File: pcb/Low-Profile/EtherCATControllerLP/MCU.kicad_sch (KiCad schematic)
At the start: 8 parts, among them U1 STM32F405RGT6, Y1 ABM3B-8.000MHZ-10-1-U-T

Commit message: checkpoint
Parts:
- U1: LCSC Part # (none) -> C15742; LCSC Part Number C15742 -> (none)
- Y1: LCSC Part # (none) -> C276420; LCSC Part Number C276420 -> (none)
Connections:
- net GND: now also U1.28 (PB2)
- net TEMP_MOSFETS: now reaches U1.15 (PA1)
- net TEMP_ICS: now reaches U1.16 (PA2)
- net TEMP_BACKSIDE: now reaches U1.17 (PA3)
- net VDD renamed VCC
- no-connect marks 19 -> 15

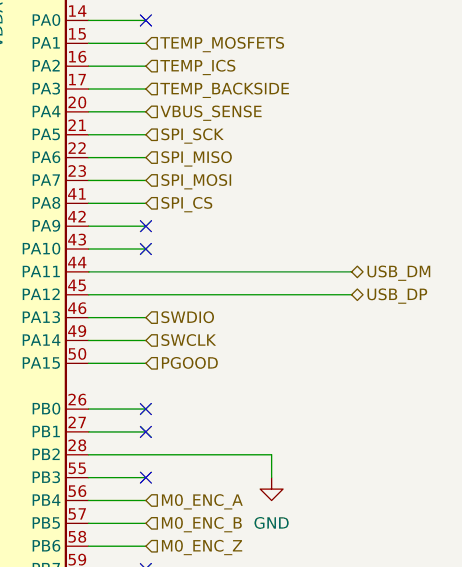
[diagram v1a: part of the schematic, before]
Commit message: Checkpoint changes before switching to XMC4800
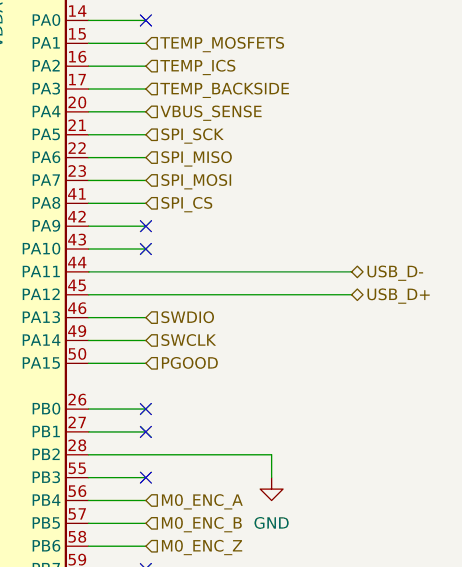
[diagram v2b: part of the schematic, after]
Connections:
- net USB_DM renamed USB_D-
- net USB_DP renamed USB_D+
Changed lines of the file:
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@@
 		)
 	)
-	(hierarchical_label "USB_DM"
+	(hierarchical_label "USB_D-"
 		(shape bidirectional)
 		(at 193.04 67.31 0)
@@
 		)
 	)
-	(hierarchical_label "USB_DP"
+	(hierarchical_label "USB_D+"
 		(shape bidirectional)
 		(at 193.04 69.85 0)

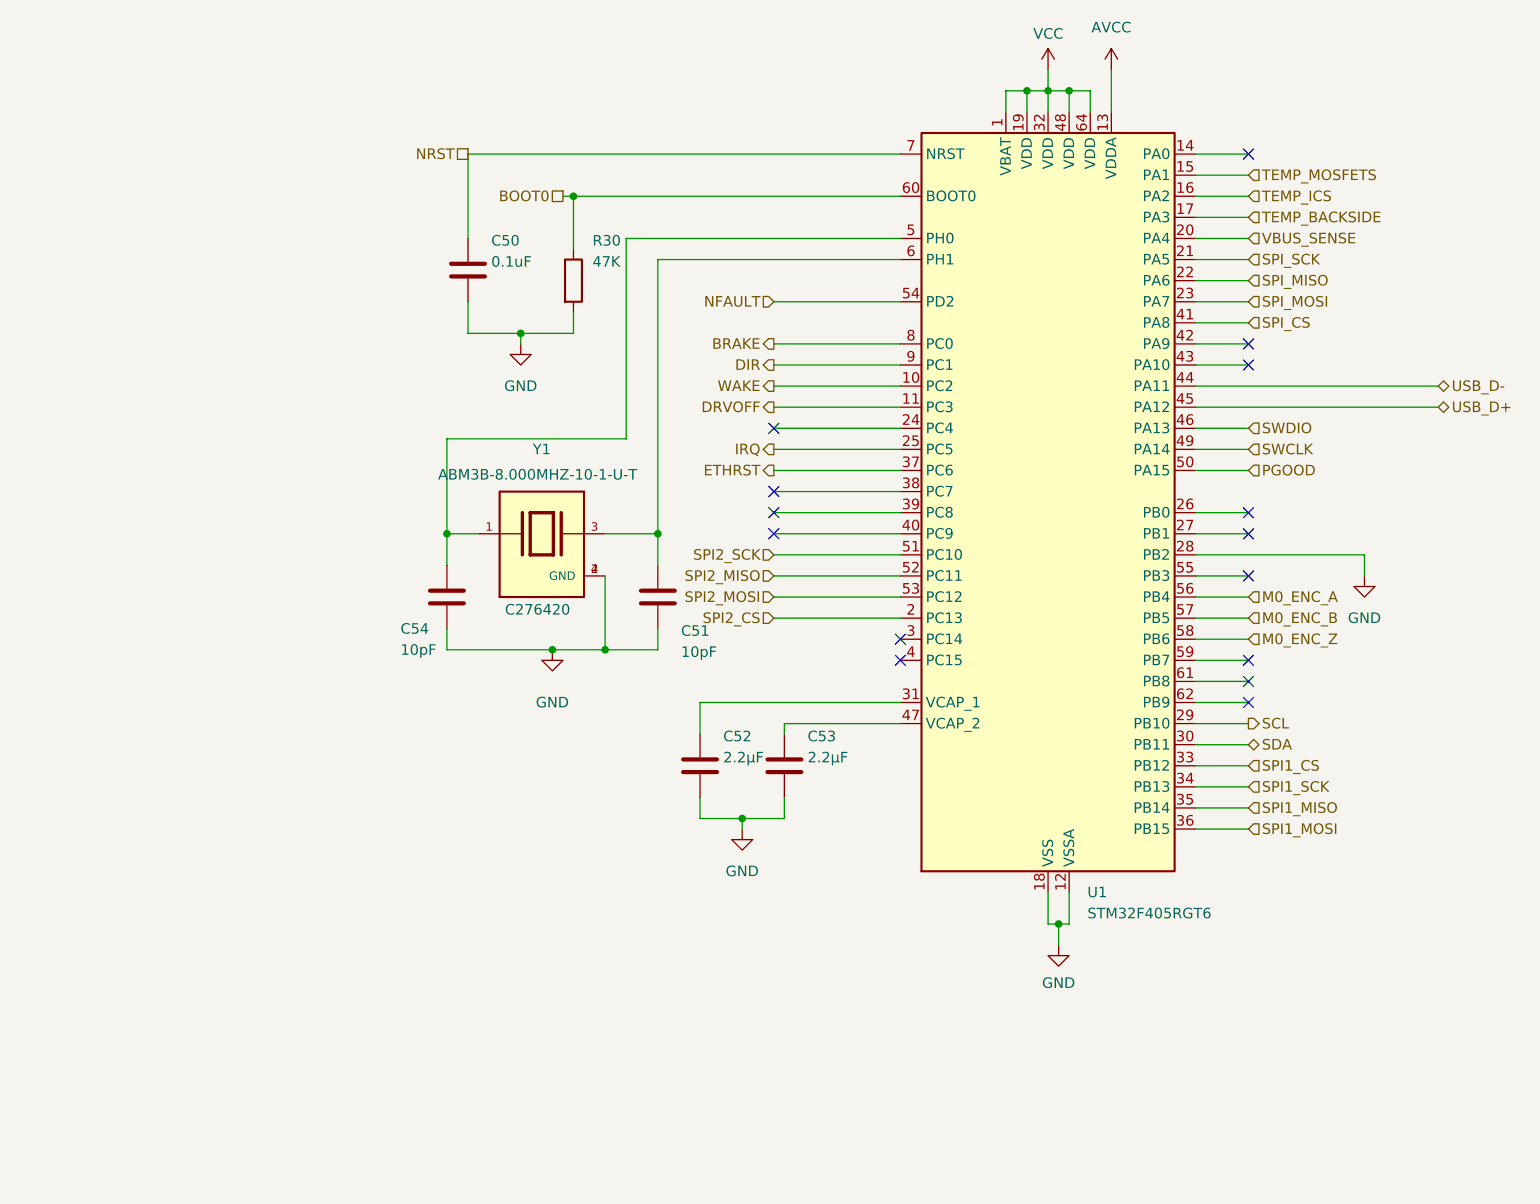
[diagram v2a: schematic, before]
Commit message: Added XMC4800
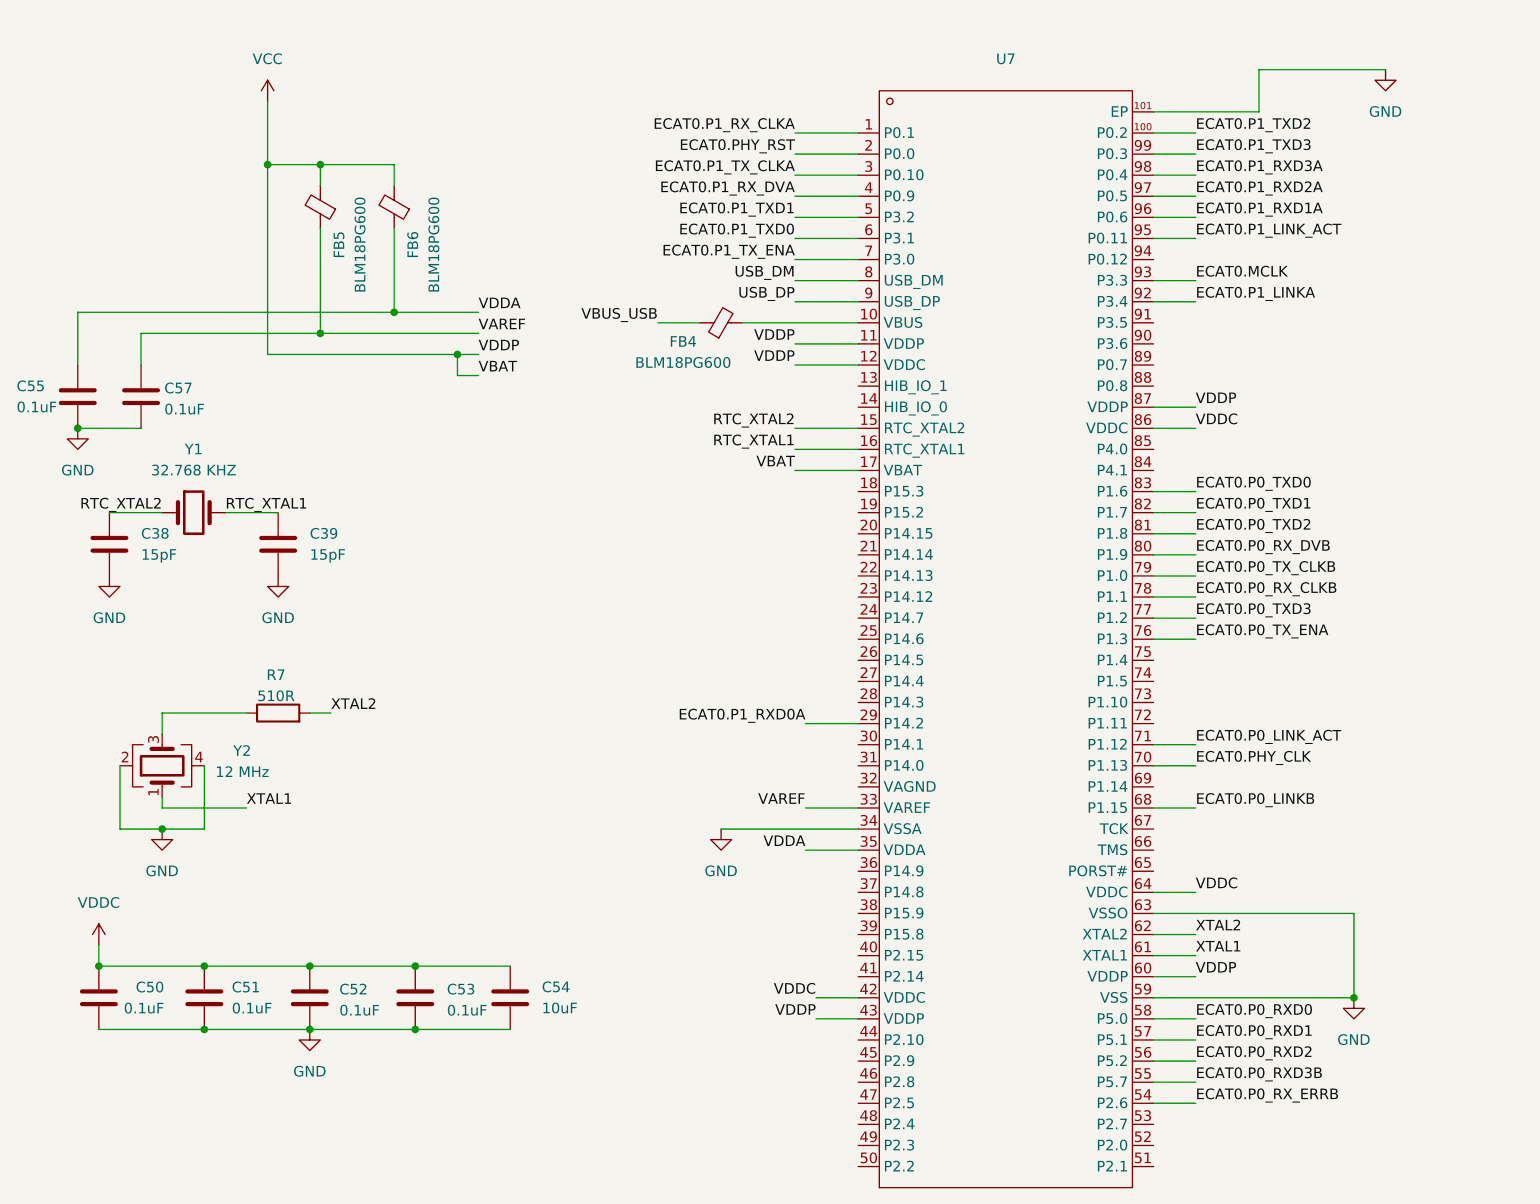
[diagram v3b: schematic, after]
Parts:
- removed R30: 47K, Resistor_SMD:R_0603_1608Metric, symbol Device:R
- removed U1: STM32F405RGT6, Package_QFP:LQFP-64_10x10mm_P0.5mm, symbol MCU_ST_STM32F4:STM32F405RGTx
- removed Y1: ABM3B-8.000MHZ-10-1-U-T, Crystal:Crystal_SMD_5032-4Pin_5.0x3.2mm, symbol ABM3B-8.000MHZ-10-1-U-T:ABM3B-8.000MHZ-10-1-U-T
- added C38, C39: 15pF, symbol Device:C
- added C55, C57: ${CAPACITANCE}, Capacitor_SMD:C_0603_1608Metric, symbol Device:C
- added FB4, FB5, FB6: BLM18PG600, symbol Device:FerriteBead_Small
- added R7: 510R, symbol Device:R
- added U7: ~, ProLibrary_pcs_2024-07-15:PG-LQFP-100_L14.0-W14.0-P0.50-LS16.0-BL-EP7.0, symbol XMC4800:XMC4800F100K1024AAXQMA1
- added Y1: 32.768 KHZ, SMD3215-2P, symbol Device:Crystal
- added Y2: 12 MHz, SMD3225-4P, symbol Device:Crystal_GND24
- C50: LCSC Part # (none) -> C77055
- C51: CAPACITANCE 10pF -> 0.1uF; COMPONENTLINK1DESCRIPTION http://www.murata.com/~/media/webrenewal/support/library/catalog/products/capacitor/mlcc/c02e.pdf -> http://www.murata.com/~/media/webrenewal/support/library/catalog/products/capacitor/mlcc/c02e.ashx?la=en-us; COMPONENTLINK1URL http://www.murata.com/~/media/webrenewal/support/library/catalog/products/capacitor/mlcc/c02e.pdf -> http://www.murata.com/~/media/webrenewal/support/library/catalog/products/capacitor/mlcc/c02e.ashx?la=en-us; LCSC Part # (none) -> C77055; MANUFACTURER PART NUMBER GRM1885C1H100JA01D -> GRM188R71H104KA93D; PACKAGING Cut Tape (CT) -> Tape & Reel (TR); PART STATUS (none) -> Active; PRICING 1 1=0.1, 10=0.041, 50=0.0222, 100=0.0187, 250=0.01532, 500=0.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 -> 4000=0.01822, 8000=0.01663, 12000=0.01584 (USD); PRICING 2 (none) -> 1=0.12, 10=0.084, 100=0.0396, 500=0.02778, 1000=0.023 (USD); SIZE / DIMENSION 0.063" L x 0.031" W (1.60mm x 0.80mm) -> 0.063" L x 0.032" W (1.60mm x 0.80mm); STOCK (none) -> 19812000; STOCK 1 450321 -> (none); SUPPLIER 2 (none) -> Digi-Key; SUPPLIER PART NUMBER 1 490-1403-1-ND -> 490-1519-2-ND; SUPPLIER PART NUMBER 2 (none) -> 490-1519-1-ND; TEMPERATURE COEFFICIENT C0G, NP0 -> X7R; TOLERANCE ±5% -> ±10%
- C52, C53: CAPACITANCE 2.2µF -> 0.1uF; COMPONENTLINK1DESCRIPTION http://www.murata.com/~/media/webrenewal/support/library/catalog/products/capacitor/mlcc/c02e.pdf -> http://www.murata.com/~/media/webrenewal/support/library/catalog/products/capacitor/mlcc/c02e.ashx?la=en-us; COMPONENTLINK1URL http://www.murata.com/~/media/webrenewal/support/library/catalog/products/capacitor/mlcc/c02e.pdf -> http://www.murata.com/~/media/webrenewal/support/library/catalog/products/capacitor/mlcc/c02e.ashx?la=en-us; LCSC Part # (none) -> C77055; MANUFACTURER PART NUMBER GRM188R61C225KE15D -> GRM188R71H104KA93D; OPERATING TEMPERATURE -55°C ~ 85°C -> -55°C ~ 125°C; PACKAGING Cut Tape (CT) -> Tape & Reel (TR); PART STATUS (none) -> Active; PRICING 1 1=0.12, 10=0.08, 50=0.046, 100=0.038, 250=0.032, 500=0.0268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 -> 4000=0.01822, 8000=0.01663, 12000=0.01584 (USD); PRICING 2 (none) -> 1=0.12, 10=0.084, 100=0.0396, 500=0.02778, 1000=0.023 (USD); SIZE / DIMENSION 0.063" L x 0.031" W (1.60mm x 0.80mm) -> 0.063" L x 0.032" W (1.60mm x 0.80mm); STOCK (none) -> 19812000; STOCK 1 1255740 -> (none); SUPPLIER 2 (none) -> Digi-Key; SUPPLIER PART NUMBER 1 490-3296-1-ND -> 490-1519-2-ND; SUPPLIER PART NUMBER 2 (none) -> 490-1519-1-ND; TEMPERATURE COEFFICIENT X5R -> X7R; VOLTAGE - RATED 16V -> 50V
- C54: value ${CAPACITANCE} -> 10uF; footprint Capacitor_SMD:C_0603_1608Metric -> (none); APPLICATIONS General Purpose -> (none); CAPACITANCE 10pF -> (none); CATEGORY Capacitors -> (none); COMPONENTLINK1DESCRIPTION http://www.murata.com/~/media/webrenewal/support/library/ca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 -> (none); COMPONENTLINK1URL http://www.murata.com/~/media/webrenewal/support/library/ca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 -> (none); FEATURES - -> (none); HEIGHT - SEATED (MAX) - -> (none); LCSC Part # (none) -> C77075; LEAD SPACING - -> (none); LEAD STYLE - -> (none); MANUFACTURER Murata Electronics North America -> (none); MANUFACTURER PART NUMBER GRM1885C1H100JA01D -> (none); MOUNTING TYPE Surface Mount, MLCC -> (none); OPERATING TEMPERATURE -55°C ~ 125°C -> (none); PACKAGE / CASE 0603 (1608 Metric) -> (none); PACKAGING Cut Tape (CT) -> (none); PRICING 1 1=0.1, 10=0.041, 50=0.0222, 100=0.0187, 250=0.01532, 500=0.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 -> (none); RATINGS - -> (none); ROHS RoHS Compliant -> (none); SIZE / DIMENSION 0.063" L x 0.031" W (1.60mm x 0.80mm) -> (none); STOCK 1 450321 -> (none); SUPPLIER 1 Digi-Key -> (none); SUPPLIER PART NUMBER 1 490-1403-1-ND -> (none); TEMPERATURE COEFFICIENT C0G, NP0 -> (none); THICKNESS (MAX) 0.035" (0.90mm) -> (none); TOLERANCE ±5% -> (none); VOLTAGE - RATED 50V -> (none)
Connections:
- net NRST is gone; now on net VDDC: C50.1
- net GND: now also C38.2, C39.2, C55.2, C57.2, U7.101 (EP), U7.34 (VSSA), U7.59 (VSS), U7.63 (VSSO), Y2.2, Y2.4
- net VCC: now also FB5.2, FB6.2, U7.11 (VDDP), U7.12 (VDDC), U7.17 (VBAT), U7.43 (VDDP), U7.60 (VDDP), U7.87 (VDDP)
- net VDDC: now reaches C53.1
- net VDDC: now also C51.1, C52.1, C54.1, U7.42 (VDDC), U7.64 (VDDC), U7.86 (VDDC)
- new net: FB4.2, U7.10 (VBUS)
- new net: R7.1, Y2.3
- new net ECAT0.MCLK: U7.93 (P3.3)
- new net ECAT0.P0_LINKB: U7.68 (P1.15)
- new net ECAT0.P0_LINK_ACT: U7.71 (P1.12)
- new net ECAT0.P0_RXD0: U7.58 (P5.0)
- new net ECAT0.P0_RXD1: U7.57 (P5.1)
- new net ECAT0.P0_RXD2: U7.56 (P5.2)
- new net ECAT0.P0_RXD3B: U7.55 (P5.7)
- new net ECAT0.P0_RX_CLKB: U7.78 (P1.1)
- new net ECAT0.P0_RX_DVB: U7.80 (P1.9)
- new net ECAT0.P0_RX_ERRB: U7.54 (P2.6)
- new net ECAT0.P0_TXD0: U7.83 (P1.6)
- new net ECAT0.P0_TXD1: U7.82 (P1.7)
- new net ECAT0.P0_TXD2: U7.81 (P1.8)
- new net ECAT0.P0_TXD3: U7.77 (P1.2)
- new net ECAT0.P0_TX_CLKB: U7.79 (P1.0)
- new net ECAT0.P0_TX_ENA: U7.76 (P1.3)
- new net ECAT0.P1_LINKA: U7.92 (P3.4)
- new net ECAT0.P1_LINK_ACT: U7.95 (P0.11)
- new net ECAT0.P1_RXD0A: U7.29 (P14.2)
- new net ECAT0.P1_RXD1A: U7.96 (P0.6)
- new net ECAT0.P1_RXD2A: U7.97 (P0.5)
- new net ECAT0.P1_RXD3A: U7.98 (P0.4)
- new net ECAT0.P1_RX_CLKA: U7.1 (P0.1)
- new net ECAT0.P1_RX_DVA: U7.4 (P0.9)
- new net ECAT0.P1_TXD0: U7.6 (P3.1)
- new net ECAT0.P1_TXD1: U7.5 (P3.2)
- new net ECAT0.P1_TXD2: U7.100 (P0.2)
- new net ECAT0.P1_TXD3: U7.99 (P0.3)
- new net ECAT0.P1_TX_CLKA: U7.3 (P0.10)
- new net ECAT0.P1_TX_ENA: U7.7 (P3.0)
- new net ECAT0.PHY_CLK: U7.70 (P1.13)
- new net ECAT0.PHY_RST: U7.2 (P0.0)
- new net RTC_XTAL1: C39.1, U7.16 (RTC_XTAL1), Y1.2
- new net RTC_XTAL2: C38.1, U7.15 (RTC_XTAL2), Y1.1
- new net USB_DM: U7.8 (USB_DM)
- new net USB_DP: U7.9 (USB_DP)
- new net VAREF: C57.1, FB5.1, U7.33 (VAREF)
- new net VBUS_USB: FB4.1
- new net VDDA: C55.1, FB6.1, U7.35 (VDDA)
- new net XTAL1: U7.61 (XTAL1), Y2.1
- new net XTAL2: R7.2, U7.62 (XTAL2)
- no-connect marks 15 -> 0

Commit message: Added Ethernet PHY
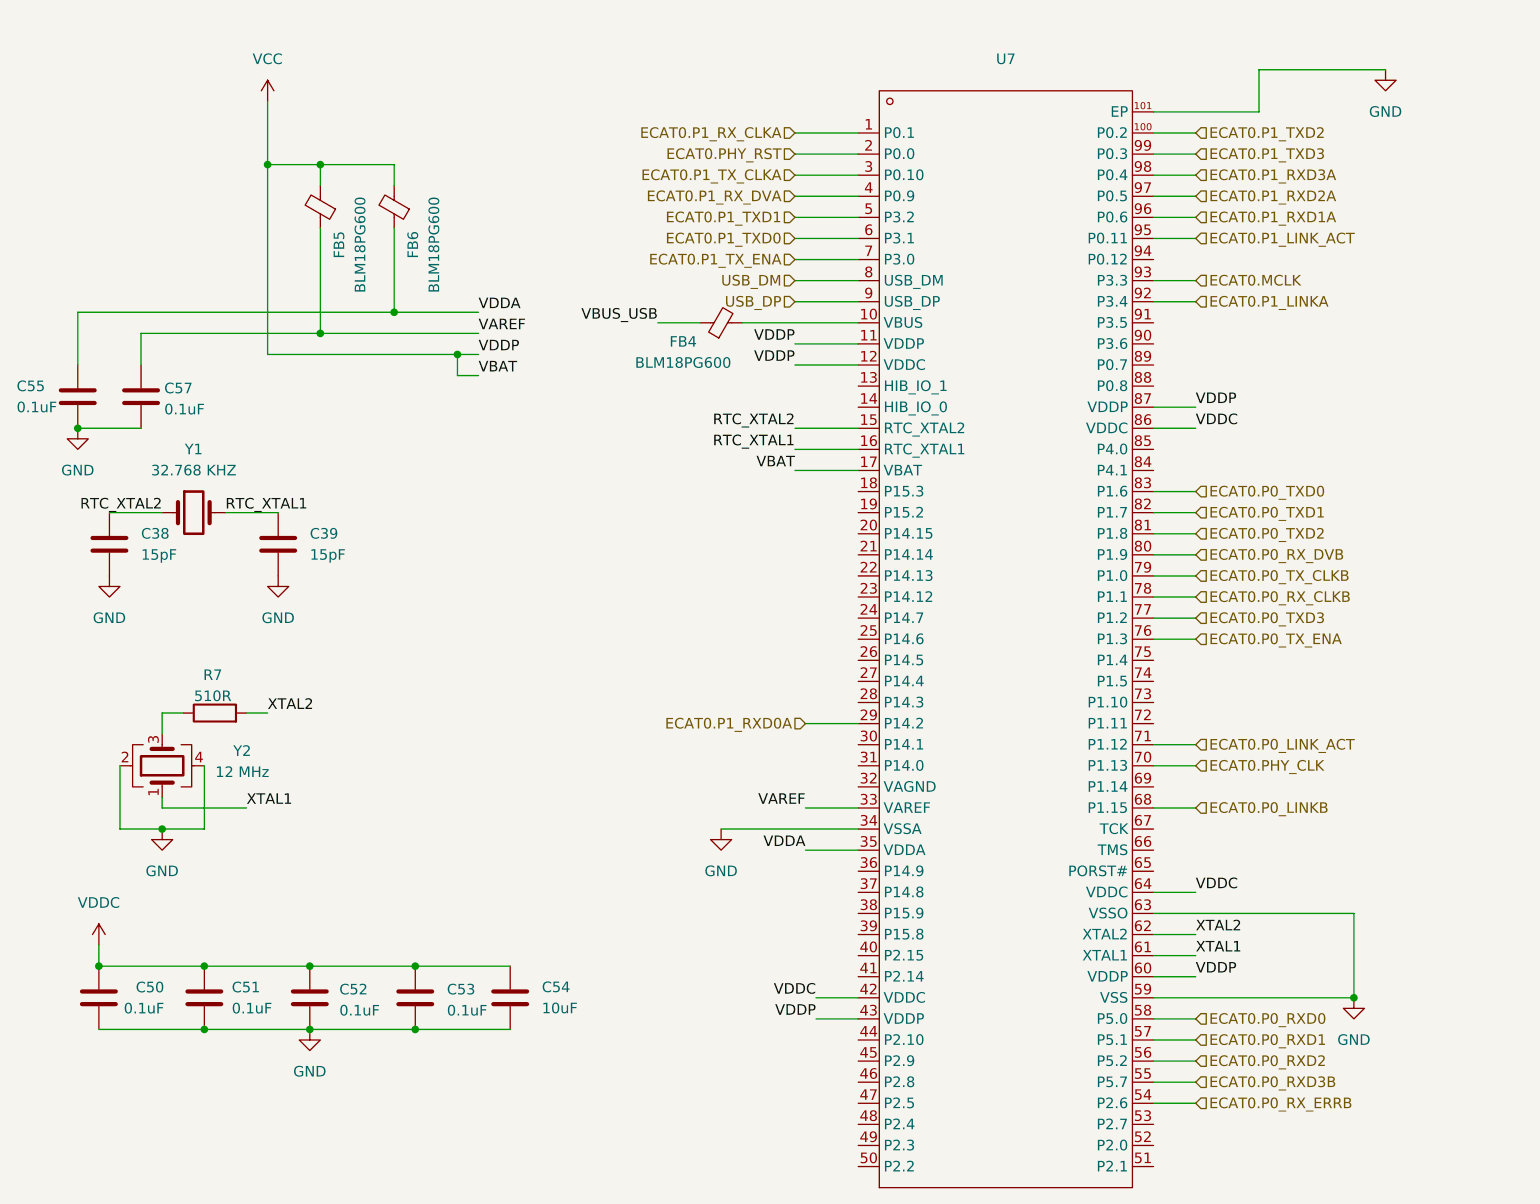
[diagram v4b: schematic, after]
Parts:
- Y1: footprint SMD3215-2P -> SMD3215-2P
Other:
- moved on the sheet: R7
